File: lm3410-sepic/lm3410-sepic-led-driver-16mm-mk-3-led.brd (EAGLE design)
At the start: 12 x 12 mm, 5 parts, among them Q1 MOSFET-NCHANNELIRLML2502

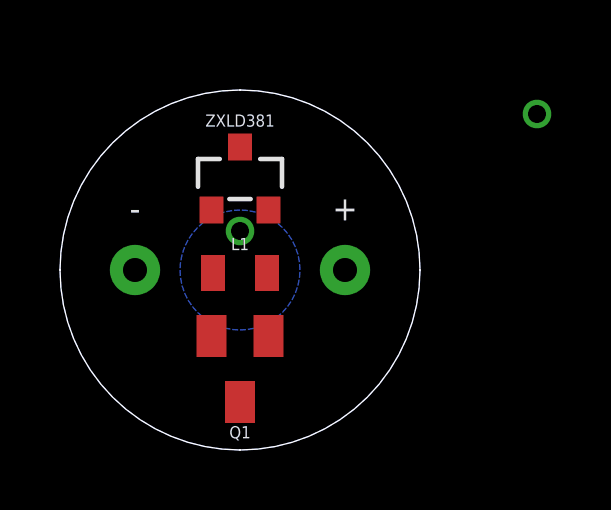
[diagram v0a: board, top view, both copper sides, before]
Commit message: bunch of new zxld38' boards and a third revision of the lm3410 pcb
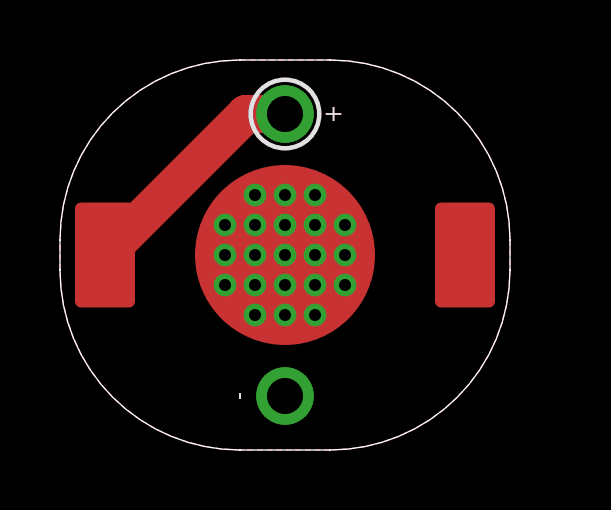
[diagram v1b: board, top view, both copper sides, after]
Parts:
- removed L1: 15uH, A_butts:0805
- removed Q1: MOSFET-NCHANNELIRLML2502, A_butts:SOT23
- removed ZXLD381: ZXLD381, A_butts:SOT23-3
- added XH-G: LEDBIG-ASS-RED-LED, A_butts:LED-GULL-WINGS-MINE-MINE-MINE
- +: value M01PTH-NS-NOTSUCK -> M01PTH-1.2MM; device A_butts:1X01NSATALL -> A_butts:1X01-1.2MM
- -: value M01PTH-NS-NOTSUCK -> M01PTH-1.2MM-NS; device A_butts:1X01NSATALL -> A_butts:1X01-1.2MM-NS
- moved - 6.53 mm to (7.50, 1.80), turned to 90 degrees
- moved + 5.57 mm to (7.50, 11.2), turned to 270 degrees
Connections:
- removed net BATT+: L1.1, Q1.1, ZXLD381.1
- removed net BATT-: Q1.3
- removed net LED+: +.1, L1.2, ZXLD381.2
- removed net LED-: -.1, Q1.2, ZXLD381.3
- new net GND: -.P$1, XH-G.K, XH-G.K@1, XH-G.K@10, XH-G.K@11, XH-G.K@12, XH-G.K@13, XH-G.K@14, XH-G.K@15, XH-G.K@16, XH-G.K@17, XH-G.K@18, XH-G.K@19, XH-G.K@20, XH-G.K@21, XH-G.K@23, XH-G.K@24, XH-G.K@25, XH-G.K@3, XH-G.K@4, XH-G.K@5, XH-G.K@7, XH-G.K@8, XH-G.K@9
- new net VCC: +.P$1, XH-G.A
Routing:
- net VCC: track 0.00 -> 7.95 mm
- added copper zone on layer 1, net GND
- added copper zone on layer 16, net GND
- removed copper zone on layer 16, net BATT+
- removed copper zone on layer 16, net BATT-
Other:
- board size 12 x 12 mm -> 15 x 13 mm
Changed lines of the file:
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@@
 <layer number="27" name="tValues" color="7" fill="1" visible="yes" active="yes"/>
 <layer number="28" name="bValues" color="7" fill="1" visible="yes" active="yes"/>
-<layer number="29" name="tStop" color="7" fill="3" visible="no" active="yes"/>
-<layer number="30" name="bStop" color="7" fill="6" visible="no" active="yes"/>
-<layer number="31" name="tCream" color="7" fill="4" visible="no" active="yes"/>
-<layer number="32" name="bCream" color="7" fill="5" visible="no" active="yes"/>
-<layer number="33" name="tFinish" color="6" fill="3" visible="no" active="yes"/>
-<layer number="34" name="bFinish" color="6" fill="6" visible="no" active="yes"/>
-<layer number="35" name="tGlue" color="7" fill="4" visible="no" active="yes"/>
-<layer number="36" name="bGlue" color="7" fill="5" visible="no" active="yes"/>
-<layer number="37" name="tTest" color="7" fill="1" visible="no" active="yes"/>
-<layer number="38" name="bTest" color="7" fill="1" visible="no" active="yes"/>
+<layer number="29" name="tStop" color="7" fill="3" visible="yes" active="yes"/>
+<layer number="30" name="bStop" color="7" fill="6" visible="yes" active="yes"/>
+<layer number="31" name="tCream" color="7" fill="4" visible="yes" active="yes"/>
+<layer number="32" name="bCream" color="7" fill="5" visible="yes" active="yes"/>
+<layer number="33" name="tFinish" color="6" fill="3" visible="yes" active="yes"/>
+<layer number="34" name="bFinish" color="6" fill="6" visible="yes" active="yes"/>
+<layer number="35" name="tGlue" color="7" fill="4" visible="yes" active="yes"/>
+<layer number="36" name="bGlue" color="7" fill="5" visible="yes" active="yes"/>
+<layer number="37" name="tTest" color="7" fill="1" visible="yes" active="yes"/>
+<layer number="38" name="bTest" color="7" fill="1" visible="yes" active="yes"/>
 <layer number="39" name="tKeepout" color="4" fill="11" visible="yes" active="yes"/>
 <layer number="40" name="bKeepout" color="1" fill="11" visible="yes" active="yes"/>
@@
 <layer number="42" name="bRestrict" color="1" fill="10" visible="yes" active="yes"/>
 <layer number="43" name="vRestrict" color="2" fill="10" visible="yes" active="yes"/>
-<layer number="44" name="Drills" color="7" fill="1" visible="no" active="yes"/>
-<layer number="45" name="Holes" color="7" fill="1" visible="no" active="yes"/>
-<layer number="46" name="Milling" color="3" fill="1" visible="no" active="yes"/>
-<layer number="47" name="Measures" color="7" fill="1" visible="no" active="yes"/>
+<layer number="44" name="Drills" color="7" fill="1" visible="yes" active="yes"/>
+<layer number="45" name="Holes" color="7" fill="1" visible="yes" active="yes"/>
+<layer number="46" name="Milling" color="3" fill="1" visible="yes" active="yes"/>
+<layer number="47" name="Measures" color="7" fill="1" visible="yes" active="yes"/>
 <layer number="48" name="Document" color="7" fill="1" visible="yes" active="yes"/>
 <layer number="49" name="Reference" color="7" fill="1" visible="yes" active="yes"/>
@@
 <board>
 <plain>
-<wire x1="6" y1="0" x2="0" y2="6" width="0" layer="20" curve="-90"/>
-<wire x1="0" y1="6" x2="6" y2="12" width="0" layer="20" curve="-90"/>
-<wire x1="6" y1="12" x2="12" y2="6" width="0" layer="20" curve="-90"/>
-<wire x1="12" y1="6" x2="6" y2="0" width="0" layer="20" curve="-90"/>
+<wire x1="0" y1="7" x2="0" y2="6" width="0" layer="20"/>
+<wire x1="0" y1="6" x2="6" y2="0" width="0" layer="20" curve="90"/>
+<wire x1="6" y1="0" x2="9" y2="0" width="0" layer="20"/>
+<wire x1="9" y1="0" x2="15" y2="6" width="0" layer="20" curve="90"/>
+<wire x1="15" y1="6" x2="15" y2="7" width="0" layer="20"/>
+<wire x1="15" y1="7" x2="9" y2="13" width="0" layer="20" curve="90"/>
+<wire x1="9" y1="13" x2="6" y2="13" width="0" layer="20"/>
+<wire x1="6" y1="13" x2="0" y2="7" width="0" layer="20" curve="90"/>
 </plain>
 <attributes>
@@
 </autorouter>
 <elements>
-<element name="ZXLD381" library="A_butts" package="SOT23-3" value="ZXLD381" x="6" y="9" smashed="yes">
-<attribute name="NAME" x="6" y="10.778" size="0.4064" layer="25" font="vector" ratio="12" align="bottom-center"/>
-</element>
-<element name="+" library="A_butts" package="1X01NSATALL" value="M01PTH-NS-NOTSUCK" x="9.5" y="6"/>
-<element name="-" library="A_butts" package="1X01NSATALL" value="M01PTH-NS-NOTSUCK" x="2.5" y="6"/>
-<element name="L1" library="A_butts" package="0805" value="15uH" x="6" y="5.9" smashed="yes">
-<attribute name="NAME" x="6" y="6.662" size="0.4064" layer="25" font="vector" ratio="12" align="bottom-center"/>
-</element>
-<element name="Q1" library="A_butts" package="SOT23" value="MOSFET-NCHANNELIRLML2502" x="6" y="2.7" smashed="yes" rot="R180">
-<attribute name="NAME" x="6" y="0.795" size="0.4064" layer="25" font="vector" ratio="12" rot="R180" align="bottom-center"/>
-</element>
+<element name="+" library="A_butts" package="1X01-1.2MM" value="M01PTH-1.2MM" x="7.5" y="11.2" rot="R270"/>
+<element name="XH-G" library="A_butts" package="LED-GULL-WINGS-MINE-MINE-MINE" value="LEDBIG-ASS-RED-LED" x="7.5" y="6.5"/>
+<element name="-" library="A_butts" package="1X01-1.2MM-NS" value="M01PTH-1.2MM-NS" x="7.5" y="1.8" rot="R90"/>
 </elements>
 <signals>
-<signal name="LED+">
-<contactref element="ZXLD381" pad="2"/>
-<contactref element="L1" pad="2"/>
-<contactref element="+" pad="1"/>
-<wire x1="6.95" y1="8" x2="9.5" y2="6" width="0" layer="19" extent="1-1"/>
-<wire x1="6.9" y1="5.9" x2="6.95" y2="8" width="0" layer="19" extent="1-1"/>
+<signal name="VCC">
+<contactref element="XH-G" pad="A"/>
+<contactref element="+" pad="P$1"/>
+<wire x1="7.5" y1="11.2" x2="6.2" y2="11.2" width="1.27" layer="1"/>
+<wire x1="6.2" y1="11.2" x2="1.5" y2="6.5" width="1.27" layer="1"/>
 </signal>
-<signal name="BATT-">
-<contactref element="Q1" pad="3"/>
-<polygon width="0.1524" layer="16" rank="6">
+<signal name="GND">
+<contactref element="XH-G" pad="K"/>
+<contactref element="XH-G" pad="K@1"/>
+<contactref element="XH-G" pad="K@3"/>
+<contactref element="XH-G" pad="K@4"/>
+<contactref element="XH-G" pad="K@5"/>
+<contactref element="XH-G" pad="K@7"/>
+<contactref element="XH-G" pad="K@8"/>
+<contactref element="XH-G" pad="K@9"/>
+<contactref element="XH-G" pad="K@10"/>
+<contactref element="XH-G" pad="K@11"/>
+<contactref element="XH-G" pad="K@12"/>
+<contactref element="XH-G" pad="K@13"/>
+<contactref element="XH-G" pad="K@14"/>
+<contactref element="XH-G" pad="K@15"/>
+<contactref element="XH-G" pad="K@16"/>
+<contactref element="XH-G" pad="K@17"/>
+<contactref element="XH-G" pad="K@18"/>
+<contactref element="XH-G" pad="K@19"/>
+<contactref element="XH-G" pad="K@20"/>
+<contactref element="XH-G" pad="K@21"/>
+<contactref element="XH-G" pad="K@23"/>
+<contactref element="XH-G" pad="K@24"/>
+<contactref element="XH-G" pad="K@25"/>
+<contactref element="-" pad="P$1"/>
+<polygon width="0.1524" layer="16">
+<vertex x="15" y="7"/>
+<vertex x="15" y="6" curve="-90"/>
+<vertex x="9" y="0"/>
 <vertex x="6" y="0" curve="-90"/>
-<vertex x="0" y="6" curve="-90"/>
-<vertex x="6" y="12" curve="-90"/>
-<vertex x="12" y="6" curve="-90"/>
+<vertex x="0" y="6"/>
+<vertex x="0" y="7" curve="-90"/>
+<vertex x="6" y="13"/>
+<vertex x="9" y="13" curve="-90"/>
 </polygon>
-<via x="15.9" y="11.2" extent="1-16" drill="0.6"/>
-<wire x1="15.9" y1="11.2" x2="6" y2="1.6" width="0" layer="19" extent="1-1"/>
-</signal>
-<signal name="LED-">
-<contactref element="Q1" pad="2"/>
-<contactref element="ZXLD381" pad="3"/>
-<contactref element="-" pad="1"/>
-<wire x1="2.5" y1="6" x2="5.05" y2="3.8" width="0" layer="19" extent="1-1"/>
-<wire x1="6" y1="10.1" x2="2.5" y2="6" width="0" layer="19" extent="1-1"/>
-</signal>
-<signal name="BATT+">
-<contactref element="ZXLD381" pad="1"/>
-<contactref element="L1" pad="1"/>
-<contactref element="Q1" pad="1"/>
-<polygon width="0.1524" layer="16">
-<vertex x="6" y="8" curve="90"/>
-<vertex x="4" y="6" curve="90"/>
-<vertex x="6" y="4" curve="90"/>
-<vertex x="8" y="6" curve="90"/>
+<polygon width="0.1524" layer="1">
+<vertex x="15" y="7"/>
+<vertex x="15" y="6" curve="-90"/>
+<vertex x="9" y="0"/>
+<vertex x="6" y="0" curve="-90"/>
+<vertex x="0" y="6"/>
+<vertex x="0" y="7" curve="-90"/>
+<vertex x="6" y="13"/>
+<vertex x="9" y="13" curve="-90"/>
 </polygon>
-<via x="6" y="7.3" extent="1-16" drill="0.6"/>
-<wire x1="6" y1="7.3" x2="5.05" y2="8" width="0" layer="19" extent="1-1"/>
-<wire x1="5.1" y1="5.9" x2="6" y2="7.3" width="0" layer="19" extent="1-1"/>
-<wire x1="6.95" y1="3.8" x2="5.1" y2="5.9" width="0" layer="19" extent="1-1"/>
 </signal>
 </signals>
